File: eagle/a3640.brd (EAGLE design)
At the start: 207 x 98 mm, 0 parts

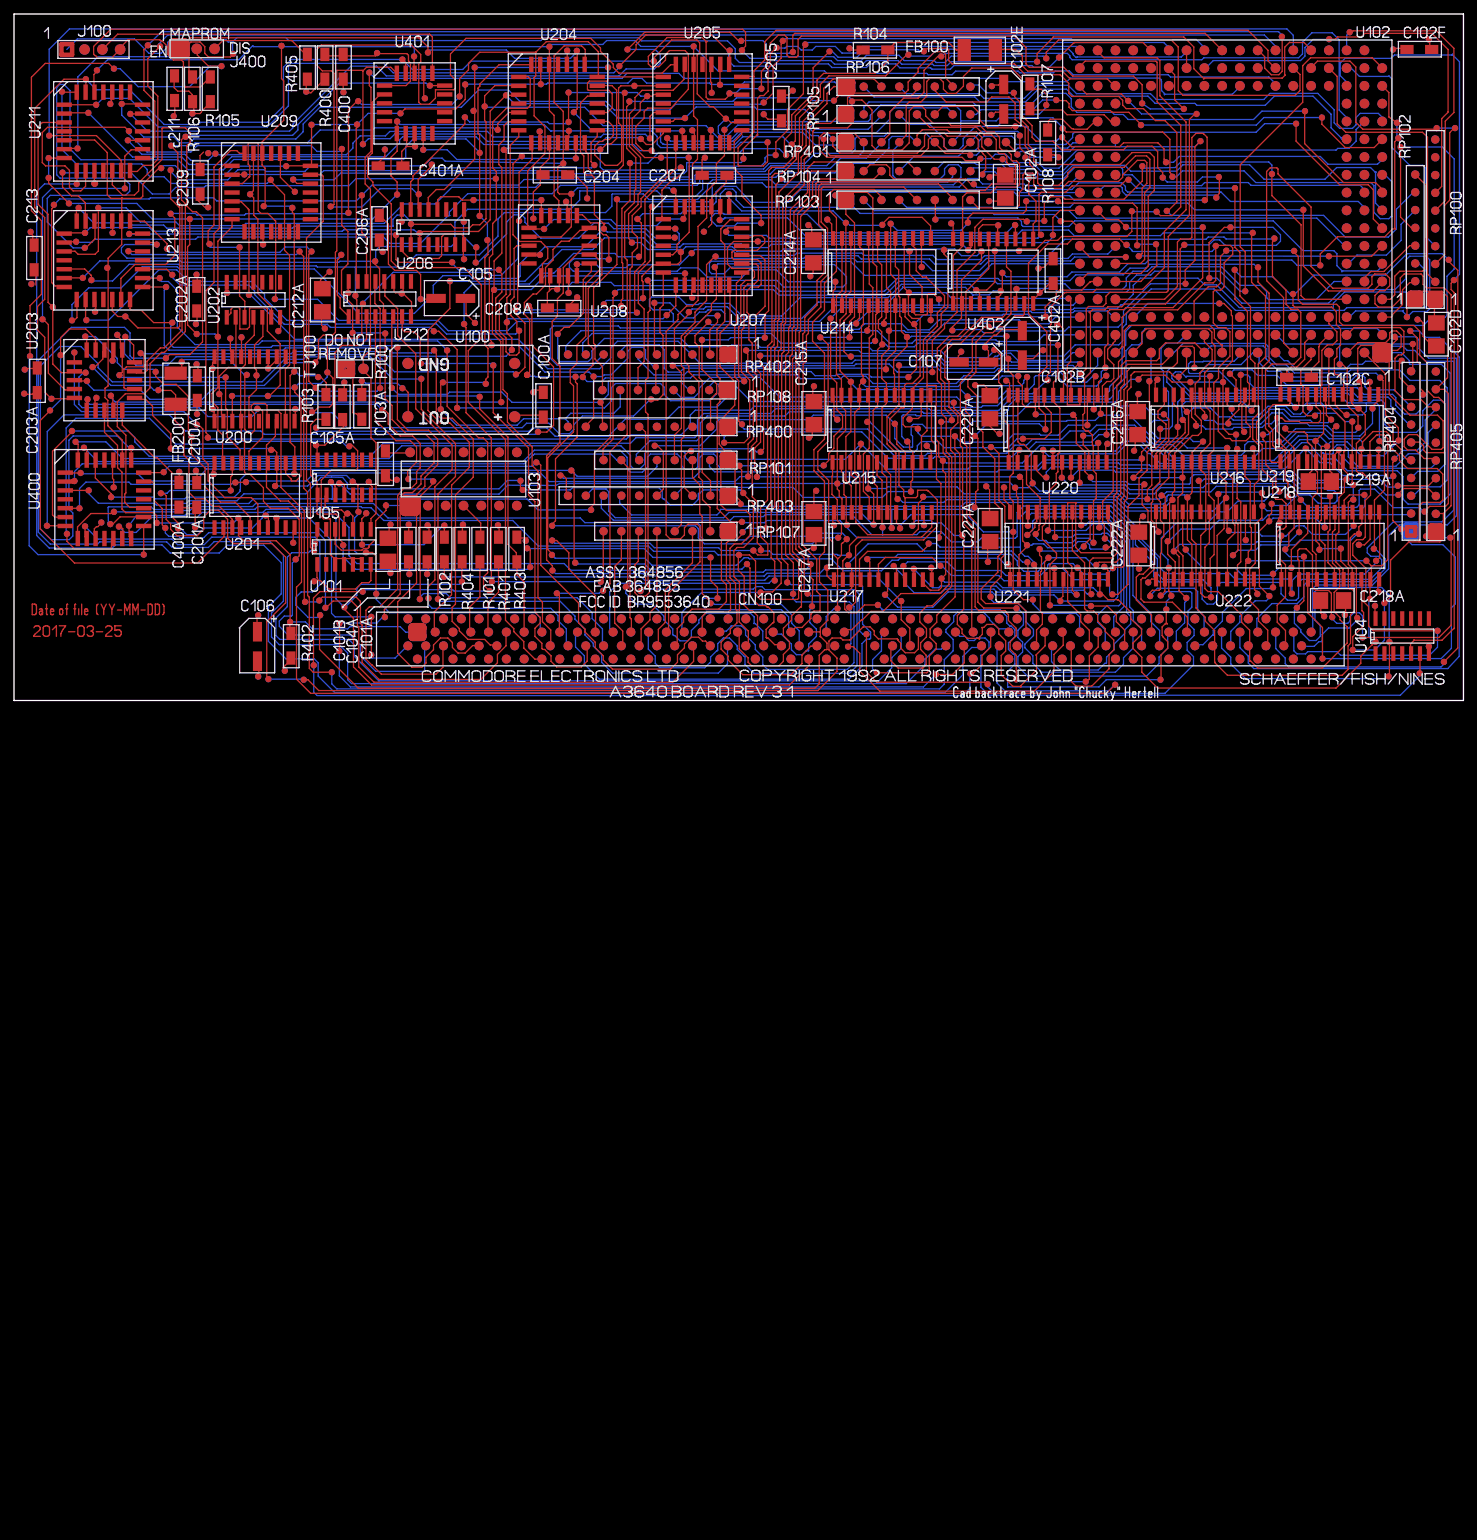
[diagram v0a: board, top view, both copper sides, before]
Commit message: placed an 040 part and wired up the data/address buses to a net.
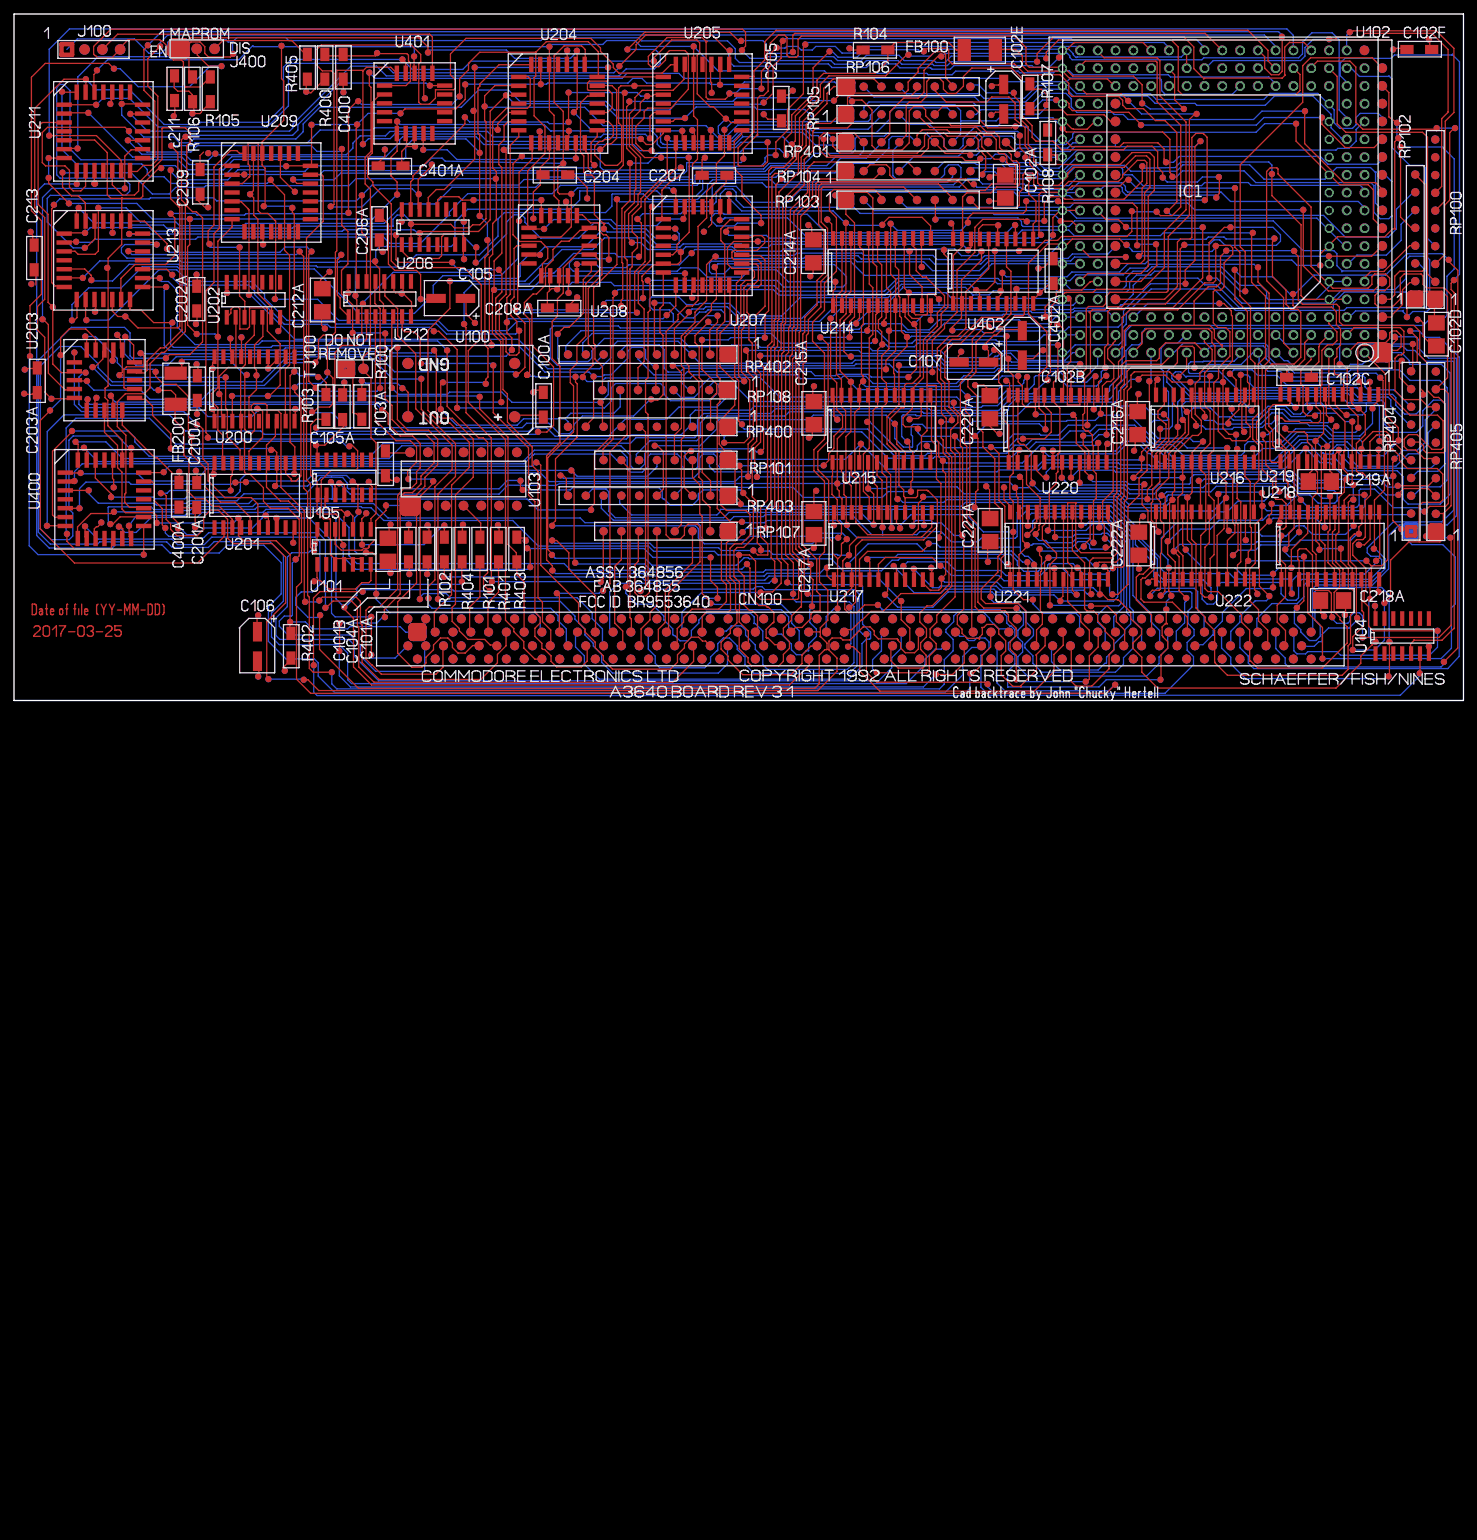
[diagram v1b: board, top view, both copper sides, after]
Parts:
- added IC1: MC68040RC, MC68K:MPGA-179
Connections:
- new net A040_0: IC1.L18
- new net A040_1: IC1.K18
- new net A040_10: IC1.P01
- new net A040_11: IC1.N03
- new net A040_12: IC1.N01
- new net A040_13: IC1.M01
- new net A040_14: IC1.L01
- new net A040_15: IC1.K01
- new net A040_16: IC1.K02
- new net A040_17: IC1.J01
- new net A040_18: IC1.H01
- new net A040_19: IC1.J02
- new net A040_2: IC1.J17
- new net A040_20: IC1.G01
- new net A040_21: IC1.F01
- new net A040_22: IC1.E01
- new net A040_23: IC1.G03
- new net A040_24: IC1.D01
- new net A040_25: IC1.F03
- new net A040_26: IC1.E02
- new net A040_27: IC1.C01
- new net A040_28: IC1.E03
- new net A040_29: IC1.B01
- new net A040_3: IC1.J18
- new net A040_30: IC1.D03
- new net A040_31: IC1.A01
- new net A040_4: IC1.H18
- new net A040_5: IC1.G18
- new net A040_6: IC1.G16
- new net A040_7: IC1.F18
- new net A040_8: IC1.E18
- new net A040_9: IC1.F16
- new net D040_0: IC1.C03
- new net D040_1: IC1.B03
- new net D040_10: IC1.A08
- new net D040_11: IC1.A09
- new net D040_12: IC1.A10
- new net D040_13: IC1.A11
- new net D040_14: IC1.A12
- new net D040_15: IC1.A13
- new net D040_16: IC1.B11
- new net D040_17: IC1.A14
- new net D040_18: IC1.B12
- new net D040_19: IC1.A15
- new net D040_2: IC1.C04
- new net D040_20: IC1.A16
- new net D040_21: IC1.A17
- new net D040_22: IC1.B16
- new net D040_23: IC1.C15
- new net D040_24: IC1.A18
- new net D040_25: IC1.C16
- new net D040_26: IC1.B18
- new net D040_27: IC1.D16
- new net D040_28: IC1.C18
- new net D040_29: IC1.E16
- new net D040_3: IC1.A02
- new net D040_30: IC1.E17
- new net D040_31: IC1.D18
- new net D040_4: IC1.A03
- new net D040_5: IC1.A04
- new net D040_6: IC1.A05
- new net D040_7: IC1.A06
- new net D040_8: IC1.B07
- new net D040_9: IC1.A07
- new net GND: IC1.B02, IC1.B04, IC1.B06, IC1.B08, IC1.B10, IC1.B13, IC1.B15, IC1.B17, IC1.C06, IC1.C07, IC1.C09, IC1.C11, IC1.C13, IC1.D02, IC1.D17, IC1.F02, IC1.F17, IC1.H02, IC1.H17, IC1.K03, IC1.K16, IC1.L02, IC1.L03, IC1.L17, IC1.M16, IC1.N02, IC1.N17, IC1.Q02, IC1.Q17, IC1.R04, IC1.R06, IC1.R10, IC1.R11, IC1.R13, IC1.S02, IC1.S09, IC1.S10, IC1.S15, IC1.S17, IC1.T04
- new net VCC: IC1.B05, IC1.B09, IC1.B14, IC1.C02, IC1.C05, IC1.C08, IC1.C10, IC1.C12, IC1.C14, IC1.C17, IC1.G02, IC1.G17, IC1.H03, IC1.H16, IC1.J03, IC1.J16, IC1.L16, IC1.M02, IC1.M03, IC1.M17, IC1.R02, IC1.R05, IC1.R08, IC1.R12, IC1.R17, IC1.S08, IC1.S16
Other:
- outline, holes or cut-outs redrawn

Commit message: chipping away at the schematic
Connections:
- new net AVEC: IC1.T11
- new net BB: IC1.T17
- new net BCLK: IC1.R07
- new net BG: IC1.T13
- new net BR: IC1.T18
- new net IPL0: IC1.T08
- new net IPL1: IC1.T07
- new net IPL2: IC1.T06
- new net PCLK: IC1.R09
- new net R/W: IC1.N16
- new net SIZ0: IC1.P17
- new net SIZ1: IC1.P16
- new net TLN0: IC1.Q18
- new net TLN1: IC1.P18
- new net TM0: IC1.N18
- new net TM1: IC1.M18
- new net TM2: IC1.K17
- new net TT0: IC1.P03
- new net TT1: IC1.P02
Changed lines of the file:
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@@
 <contactref element="IC1" pad="A01"/>
+</signal>
+<signal name="IPL0">
+<contactref element="IC1" pad="T08"/>
+</signal>
+<signal name="IPL1">
+<contactref element="IC1" pad="T07"/>
+</signal>
+<signal name="IPL2">
+<contactref element="IC1" pad="T06"/>
+</signal>
+<signal name="BR">
+<contactref element="IC1" pad="T18"/>
+</signal>
+<signal name="BG">
+<contactref element="IC1" pad="T13"/>
+</signal>
+<signal name="BB">
+<contactref element="IC1" pad="T17"/>
+</signal>
+<signal name="BCLK">
+<contactref element="IC1" pad="R07"/>
+</signal>
+<signal name="PCLK">
+<contactref element="IC1" pad="R09"/>
+</signal>
+<signal name="TT0">
+<contactref element="IC1" pad="P03"/>
+</signal>
+<signal name="TT1">
+<contactref element="IC1" pad="P02"/>
+</signal>
+<signal name="TM0">
+<contactref element="IC1" pad="N18"/>
+</signal>
+<signal name="TM1">
+<contactref element="IC1" pad="M18"/>
+</signal>
+<signal name="TM2">
+<contactref element="IC1" pad="K17"/>
+</signal>
+<signal name="TLN0">
+<contactref element="IC1" pad="Q18"/>
+</signal>
+<signal name="TLN1">
+<contactref element="IC1" pad="P18"/>
+</signal>
+<signal name="SIZ0">
+<contactref element="IC1" pad="P17"/>
+</signal>
+<signal name="SIZ1">
+<contactref element="IC1" pad="P16"/>
+</signal>
+<signal name="R/W">
+<contactref element="IC1" pad="N16"/>
+</signal>
+<signal name="AVEC">
+<contactref element="IC1" pad="T11"/>
 </signal>
 </signals>

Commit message: More stuff.
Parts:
- added U214, U215, U216, U217, U218, U219, U220, U221: 74FCT543, terriblefire:SOIC24L
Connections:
- net D040_0: now also U218.3, U219.3, U220.3
- net D040_1: now also U218.4, U219.4, U220.4
- net D040_10: now also U217.5, U221.5
- net D040_11: now also U217.6, U221.6
- net D040_12: now also U217.7, U221.7
- net D040_13: now also U217.8, U221.8
- net D040_14: now also U217.9, U221.9
- net D040_15: now also U217.10, U221.10
- net D040_16: now also U215.3, U216.3
- net D040_17: now also U215.4, U216.4
- net D040_18: now also U215.5, U216.5
- net D040_19: now also U215.6, U216.6
- net D040_2: now also U218.5, U219.5, U220.5
- net D040_20: now also U215.7, U216.7
- net D040_21: now also U215.8, U216.8
- net D040_22: now also U215.9, U216.9
- net D040_23: now also U215.10, U216.10
- net D040_24: now also U214.3
- net D040_25: now also U214.4
- net D040_26: now also U214.5
- net D040_27: now also U214.6
- net D040_28: now also U214.7
- net D040_29: now also U214.8
- net D040_3: now also U218.6, U219.6, U220.6
- net D040_30: now also U214.9
- net D040_31: now also U214.10
- net D040_4: now also U218.7, U219.7, U220.7
- net D040_5: now also U218.8, U219.8, U220.8
- net D040_6: now also U218.9, U219.9, U220.9
- net D040_7: now also U218.10, U219.10, U220.10
- net D040_8: now also U217.3, U221.3
- net D040_9: now also U217.4, U221.4
- net GND: now also U214.12, U215.12, U216.12, U217.12, U218.12, U219.12, U220.12, U221.12
- net VCC: now also U214.24, U215.24, U216.24, U217.24, U218.24, U219.24, U220.24, U221.24
